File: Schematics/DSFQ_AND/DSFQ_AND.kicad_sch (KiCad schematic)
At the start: 24 parts

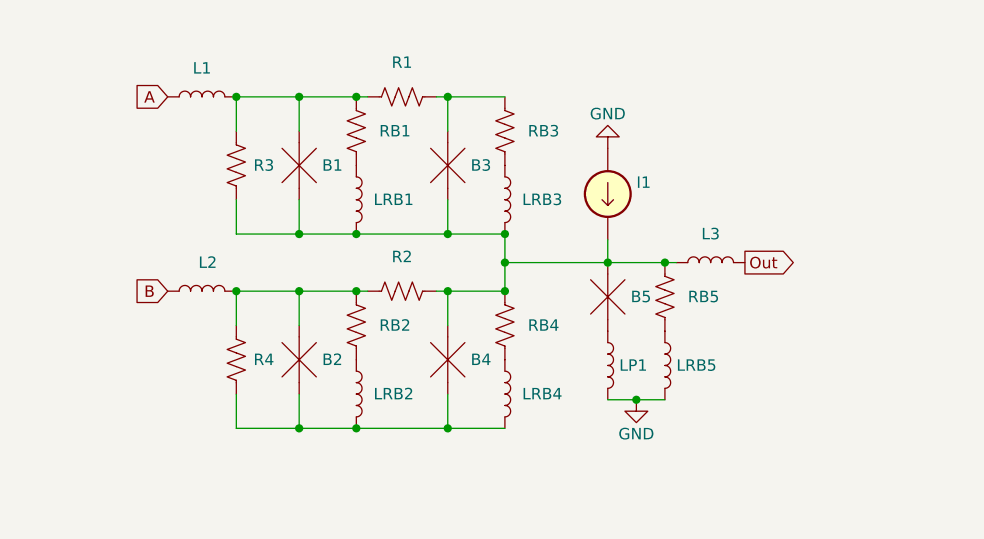
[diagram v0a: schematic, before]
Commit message: AND v1.3
Improvements to the AND gate which include version 1.3, and it's optimized version with a critical margin of 22%
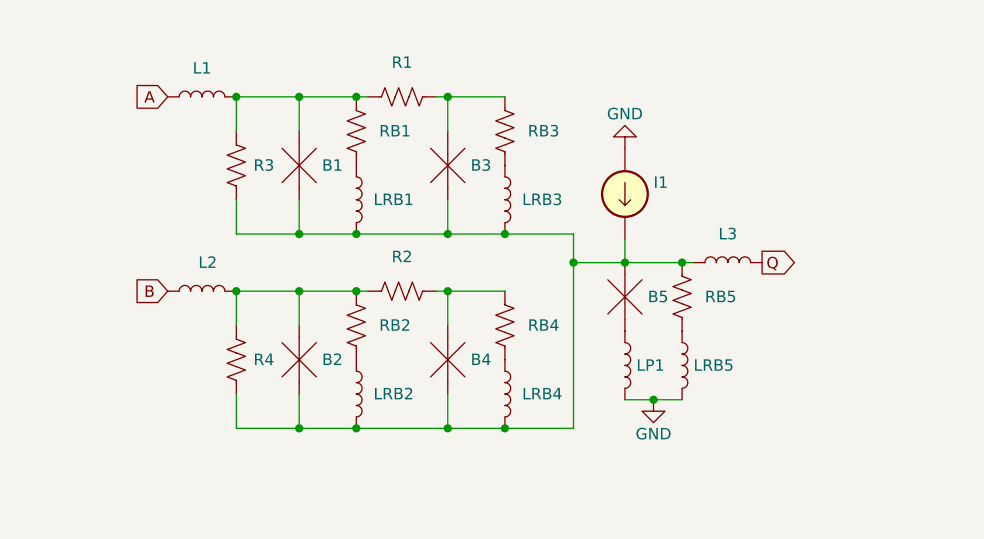
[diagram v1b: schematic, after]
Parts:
- I1: Spice_Model pwl(0 0 100u) -> pwl(0 0 5p REF)
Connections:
- net at B2.1, B4.1, LRB2.2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: now also B1.1, B3.1, B5.2, I1.2, L3.1, LRB1.2, LRB3.2, R3.2, RB5.1
- net Out renamed Q
- new net: B4.2, R2.1, RB4.1
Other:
- moved on the sheet: B5, I1, L3, LP1, LRB5, RB5

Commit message: AND Layout v1.0
Initial publication of my DSFQ AND gate layout. Optimized, It has about a 22% critical margin.
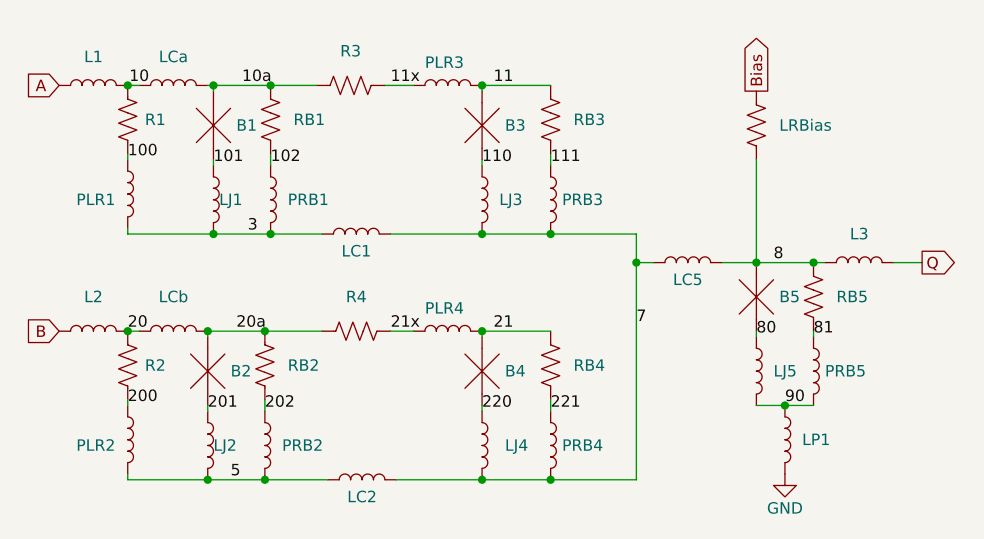
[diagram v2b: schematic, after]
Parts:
- removed I1: Current_Source, symbol Superconductors:Current_Source
- removed LRB2, LRB4: Inductor, symbol Superconductors:Inductor
- added LC1, LC2, LC5, LCa, LCb, LJ1, LJ2, LJ3, LJ4, LJ5, PLR1, PLR2, PLR3, PLR4, PRB2, PRB4: Inductor, symbol Superconductors:Inductor
- added LRBias: Resistor, symbol Superconductors:Resistor
- renumbered LRB1 to PRB1, LRB3 to PRB3, LRB5 to PRB5, R3 to R1, R1 to R3
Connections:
- net GND: no longer PRB5.2
- net 81: now reaches PRB5.1, RB5.2
- net 202: now reaches RB2.2
- net 202: now also PRB2.1
- net 10a: now reaches B1.2, R3.2, RB1.1
- net 10a: now also LCa.2; no longer L1.2, R1.1
- net 21: now reaches B4.2, RB4.1
- net 21: now also PLR4.2; no longer R2.1
- net 221: now reaches RB4.2
- net 221: now also PRB4.1
- net 11: now reaches B3.2, RB3.1
- net 11: now also PLR3.2; no longer R3.1
- net 111: now reaches PRB3.1, RB3.2
- net 80: now reaches B5.1
- net 80: now also LJ5.1; no longer LP1.1
- net 102: now reaches PRB1.1, RB1.2
- new net 10: L1.2, LCa.1, R1.1
- new net 100: PLR1.1, R1.2
- new net 101: B1.1, LJ1.1
- new net 110: B3.1, LJ3.1
- new net 11x: PLR3.1, R3.1
- new net 20: L2.2, LCb.1, R2.1
- new net 200: PLR2.1, R2.2
- new net 201: B2.1, LJ2.1
- new net 20a: B2.2, LCb.2, R4.2, RB2.1
- new net 21x: PLR4.1, R4.1
- new net 220: B4.1, LJ4.1
- new net 3: LC1.1, LJ1.2, PLR1.2, PRB1.2
- new net 5: LC2.1, LJ2.2, PLR2.2, PRB2.2
- new net 7: LC1.2, LC2.2, LC5.1, LJ3.2, LJ4.2, PRB3.2, PRB4.2
- new net 8: B5.2, L3.1, LC5.2, LRBias.2, RB5.1
- new net 90: LJ5.2, LP1.1, PRB5.2
- new net Bias: LRBias.1
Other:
- moved on the sheet: B1, B3, B5, L1, L3, PRB1, PRB3, PRB5, R1, R3, RB1, RB3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
